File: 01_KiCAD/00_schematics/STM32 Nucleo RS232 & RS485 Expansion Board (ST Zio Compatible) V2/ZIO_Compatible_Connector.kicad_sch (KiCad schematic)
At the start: 15 parts, among them CN10 Conn_02x17_Odd_Even, CN7 Conn_02x10_Odd_Even, CN8 Conn_02x08_Odd_Even, CN9 Conn_02x15_Odd_Even, Q2 BSS84

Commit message: Finishing up the schematic aand created the board outline
Made some finishing touches to the schematic, updated all the symbol footprints and started to create the board.
Added missing 3D models for Phoenix 4-p RS485 connector and RS232 connector, also for Inolux LED.
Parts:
- CN10: footprint (none) -> SSW-117-23-F-D:SAMTEC_SSW-117-23-F-D
- CN7: footprint (none) -> SSW-110-23-X-D:SAMTEC_SSW-110-23-X-D
- CN8: footprint (none) -> SSW-108-23-F-D:SAMTEC_SSW-108-23-F-D
- renumbered R34 to R70, R35 to R71, R36 to R72, R37 to R73, R38 to R74, R39 to R75, R40 to R76, R41 to R77, R42 to R78, R43 to R79
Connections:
- net MCU_SHDN_N_1 renamed MCU_SHDN
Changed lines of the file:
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@@
 		)
 	)
-	(global_label "MCU_SHDN_N_1"
+	(global_label "MCU_SHDN"
 		(shape output)
 		(at 118.11 133.35 0)
@@
 		)
 		(property "Intersheetrefs" "${INTERSHEET_REFS}"
-			(at 135.7304 133.35 0)
+			(at 131.2552 133.35 0)
 			(effects
 				(font
@@
 		(on_board yes)
 		(dnp no)
-		(property "Reference" "R37"
+		(property "Reference" "R73"
 			(at 82.55 96.52 90)
 			(effects
@@
 			(project "STM32 Nucleo RS232 & RS485 Expansion Board (ST Zio Compatible) V2"
 				(path "/080f83b7-8913-48e8-ab8e-79cb12295542/067a36dd-1222-49fa-b4c7-0b289d0be8ff"
-					(reference "R37")
+					(reference "R73")
 					(unit 1)
 				)
@@
 		(on_board yes)
 		(dnp no)
-		(property "Reference" "R38"
+		(property "Reference" "R74"
 			(at 66.04 101.6 90)
 			(effects
@@
 			(project "STM32 Nucleo RS232 & RS485 Expansion Board (ST Zio Compatible) V2"
 				(path "/080f83b7-8913-48e8-ab8e-79cb12295542/067a36dd-1222-49fa-b4c7-0b289d0be8ff"
-					(reference "R38")
+					(reference "R74")
 					(unit 1)
 				)
@@
 		(on_board yes)
 		(dnp no)
-		(property "Reference" "R43"
+		(property "Reference" "R79"
 			(at 147.574 255.27 90)
 			(effects
@@
 			(project "STM32 Nucleo RS232 & RS485 Expansion Board (ST Zio Compatible) V2"
 				(path "/080f83b7-8913-48e8-ab8e-79cb12295542/067a36dd-1222-49fa-b4c7-0b289d0be8ff"
-					(reference "R43")
+					(reference "R79")
 					(unit 1)
 				)
@@
 			)
 		)
-		(property "Datasheet" "https://www.lcsc.com/datasheet/C7089189.pdf"
+		(property "Datasheet" "~"
 			(at 104.14 115.57 0)
 			(effects
@@
 			)
 		)
-		(property "Description" "Female Header 30 Position 2.54mm Pitch Dual Row Through Hole -55℃~+125℃"
+		(property "Description" "Generic connector, double row, 02x15, odd/even pin numbering scheme (row 1 odd numbers, row 2 even numbers), script generated (kicad-library-utils/schlib/autogen/connector/)"
 			(at 104.14 115.57 0)
 			(effects
@@
 		(on_board yes)
 		(dnp no)
-		(property "Reference" "R35"
+		(property "Reference" "R71"
 			(at 193.04 76.2 90)
 			(effects
@@
 			(project "STM32 Nucleo RS232 & RS485 Expansion Board (ST Zio Compatible) V2"
 				(path "/080f83b7-8913-48e8-ab8e-79cb12295542/067a36dd-1222-49fa-b4c7-0b289d0be8ff"
-					(reference "R35")
+					(reference "R71")
 					(unit 1)
 				)
@@
 		(on_board yes)
 		(dnp no)
-		(property "Reference" "R39"
+		(property "Reference" "R75"
 			(at 82.55 104.14 90)
 			(effects
@@
 			(project "STM32 Nucleo RS232 & RS485 Expansion Board (ST Zio Compatible) V2"
 				(path "/080f83b7-8913-48e8-ab8e-79cb12295542/067a36dd-1222-49fa-b4c7-0b289d0be8ff"
-					(reference "R39")
+					(reference "R75")
 					(unit 1)
 				)
@@
 		(on_board yes)
 		(dnp no)
-		(property "Reference" "R40"
+		(property "Reference" "R76"
 			(at 76.2 109.22 90)
 			(effects
@@
 			(project "STM32 Nucleo RS232 & RS485 Expansion Board (ST Zio Compatible) V2"
 				(path "/080f83b7-8913-48e8-ab8e-79cb12295542/067a36dd-1222-49fa-b4c7-0b289d0be8ff"
-					(reference "R40")
+					(reference "R76")
 					(unit 1)
 				)
@@
 		(on_board yes)
 		(dnp no)
-		(property "Reference" "R34"
+		(property "Reference" "R70"
 			(at 193.04 63.5 90)
 			(effects
@@
 			(project "STM32 Nucleo RS232 & RS485 Expansion Board (ST Zio Compatible) V2"
 				(path "/080f83b7-8913-48e8-ab8e-79cb12295542/067a36dd-1222-49fa-b4c7-0b289d0be8ff"
-					(reference "R34")
+					(reference "R70")
 					(unit 1)
 				)
@@
 		(dnp no)
 		(fields_autoplaced yes)
-		(property "Reference" "R41"
+		(property "Reference" "R77"
 			(at 139.7 228.5999 0)
 			(effects
@@
 			(project "STM32 Nucleo RS232 & RS485 Expansion Board (ST Zio Compatible) V2"
 				(path "/080f83b7-8913-48e8-ab8e-79cb12295542/067a36dd-1222-49fa-b4c7-0b289d0be8ff"
-					(reference "R41")
+					(reference "R77")
 					(unit 1)
 				)
@@
 			)
 		)
-		(property "Footprint" ""
+		(property "Footprint" "SSW-110-23-X-D:SAMTEC_SSW-110-23-X-D"
 			(at 181.61 64.77 0)
 			(effects
@@
 			)
 		)
-		(property "Datasheet" "https://www.lcsc.com/datasheet/C6236460.pdf"
+		(property "Datasheet" "~"
 			(at 181.61 64.77 0)
 			(effects
@@
 			)
 		)
-		(property "Description" "-55℃~+125℃ Through Hole 4.7A 20P 8.51mm 2.54mm 2 2.54mm Through Hole,P=2.54mm Headers, Receptacles, Female Sockets RoHS"
+		(property "Description" "Generic connector, double row, 02x10, odd/even pin numbering scheme (row 1 odd numbers, row 2 even numbers), script generated (kicad-library-utils/schlib/autogen/connector/)"
 			(at 181.61 64.77 0)
 			(effects
@@
 			)
 		)
-		(property "Footprint" ""
+		(property "Footprint" "SSW-108-23-F-D:SAMTEC_SSW-108-23-F-D"
 			(at 104.14 72.39 0)
 			(effects
@@
 			)
 		)
-		(property "Datasheet" "https://www.lcsc.com/datasheet/C7019040.pdf"
+		(property "Datasheet" "~"
 			(at 104.14 72.39 0)
 			(effects
@@
 			)
 		)
-		(property "Description" "-55℃~+125℃ Through Hole 4.7A 16P 8.51mm 2.54mm 2 2.54mm Through Hole,P=2.54mm Headers, Receptacles, Female Sockets RoHS"
+		(property "Description" "Generic connector, double row, 02x08, odd/even pin numbering scheme (row 1 odd numbers, row 2 even numbers), script generated (kicad-library-utils/schlib/autogen/connector/)"
 			(at 104.14 72.39 0)
 			(effects
@@
 		(dnp no)
 		(fields_autoplaced yes)
-		(property "Reference" "#PWR047"
+		(property "Reference" "#PWR067"
 			(at 92.71 88.9 0)
 			(effects
@@
 			(project ""
 				(path "/080f83b7-8913-48e8-ab8e-79cb12295542/067a36dd-1222-49fa-b4c7-0b289d0be8ff"
-					(reference "#PWR047")
+					(reference "#PWR067")
 					(unit 1)
 				)
@@
 		(on_board yes)
 		(dnp no)
-		(property "Reference" "R36"
+		(property "Reference" "R72"
 			(at 193.04 91.44 90)
 			(effects
@@
 			(project "STM32 Nucleo RS232 & RS485 Expansion Board (ST Zio Compatible) V2"
 				(path "/080f83b7-8913-48e8-ab8e-79cb12295542/067a36dd-1222-49fa-b4c7-0b289d0be8ff"
-					(reference "R36")
+					(reference "R72")
 					(unit 1)
 				)
@@
 			)
 		)
-		(property "Footprint" ""
+		(property "Footprint" "SSW-117-23-F-D:SAMTEC_SSW-117-23-F-D"
 			(at 181.61 113.03 0)
 			(effects
@@
 			)
 		)
-		(property "Datasheet" "https://www.lcsc.com/datasheet/C6501751.pdf"
+		(property "Datasheet" "~"
 			(at 181.61 113.03 0)
 			(effects
@@
 			)
 		)
-		(property "Description" "Female Header 34 Position 2.54mm Pitch Dual Row Through Hole -55℃~+125℃"
+		(property "Description" "Generic connector, double row, 02x17, odd/even pin numbering scheme (row 1 odd numbers, row 2 even numbers), script generated (kicad-library-utils/schlib/autogen/connector/)"
 			(at 181.61 113.03 0)
 			(effects
@@
 		(dnp no)
 		(fields_autoplaced yes)
-		(property "Reference" "R42"
+		(property "Reference" "R78"
 			(at 162.56 228.5999 0)
 			(effects
@@
 			(project "STM32 Nucleo RS232 & RS485 Expansion Board (ST Zio Compatible) V2"
 				(path "/080f83b7-8913-48e8-ab8e-79cb12295542/067a36dd-1222-49fa-b4c7-0b289d0be8ff"
-					(reference "R42")
+					(reference "R78")
 					(unit 1)
 				)

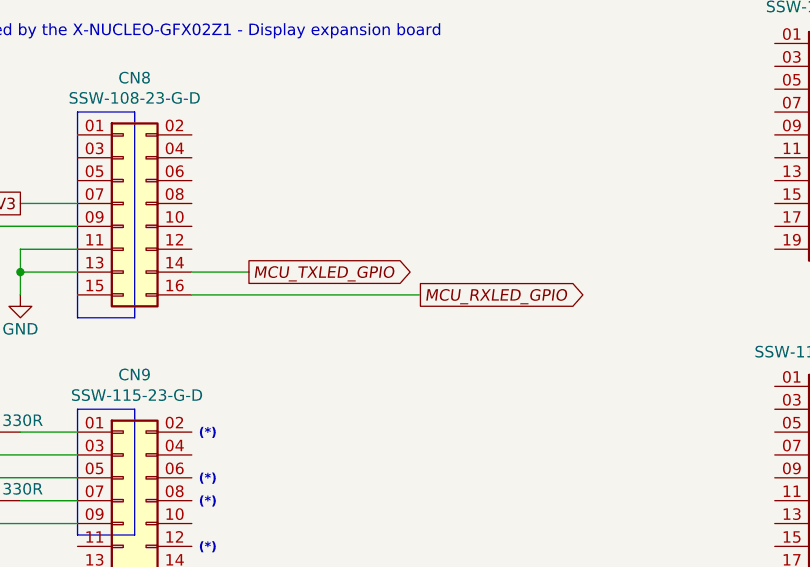
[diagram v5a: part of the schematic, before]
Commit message: Updated footprints and added components to PCB
Added some additional components to the board. Changed the footprint of the 3-pin Jumper so the bottom silkscreen text doesnlt overlap with the Dual Schmidt Trigger IC's SN74LVC2G14
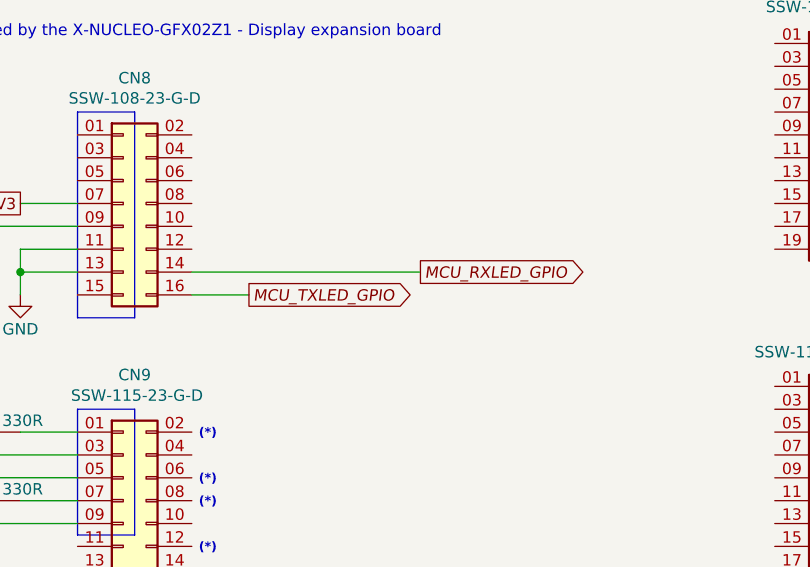
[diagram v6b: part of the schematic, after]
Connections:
- net MCU_RXLED_GPIO: now also CN8.14 (Pin_14); no longer CN8.16 (Pin_16)
- net MCU_TXLED_GPIO: now also CN8.16 (Pin_16); no longer CN8.14 (Pin_14)
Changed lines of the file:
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@@
 	(wire
 		(pts
-			(xy 217.17 64.77) (xy 203.2 64.77)
+			(xy 111.76 82.55) (xy 118.11 82.55)
 		)
 		(stroke
@@
 	(wire
 		(pts
-			(xy 111.76 80.01) (xy 118.11 80.01)
+			(xy 217.17 64.77) (xy 203.2 64.77)
 		)
 		(stroke
@@
 	(wire
 		(pts
+			(xy 111.76 80.01) (xy 137.16 80.01)
+		)
+		(stroke
+			(width 0)
+			(type default)
+		)
+	)
+	(wire
+		(pts
 			(xy 208.28 92.71) (xy 203.2 92.71)
 		)
@@
 		)
 	)
-	(wire
-		(pts
-			(xy 111.76 82.55) (xy 137.16 82.55)
-		)
-		(stroke
-			(width 0)
-			(type default)
-		)
-	)
 	(global_label "L3-TXD"
 		(shape output)
@@
 	(global_label "MCU_RXLED_GPIO"
 		(shape output)
-		(at 137.16 82.55 0)
+		(at 137.16 80.01 0)
 		(fields_autoplaced yes)
 		(effects
@@
 		)
 		(property "Intersheetrefs" "${INTERSHEET_REFS}"
-			(at 156.5342 82.55 0)
+			(at 156.5342 80.01 0)
 			(effects
 				(font
@@
 	(global_label "MCU_TXLED_GPIO"
 		(shape output)
-		(at 118.11 80.01 0)
+		(at 118.11 82.55 0)
 		(fields_autoplaced yes)
 		(effects
@@
 		)
 		(property "Intersheetrefs" "${INTERSHEET_REFS}"
-			(at 137.1818 80.01 0)
+			(at 137.1818 82.55 0)
 			(effects
 				(font
@@
 			)
 		)
-		(property "Datasheet" "https://www.lcsc.com/datasheet/C105881.pdf"
+		(property "Datasheet" "~"
 			(at 87.63 97.79 0)
 			(effects
@@
 			)
 		)
-		(property "Description" "100mW 330Ω 75V Thick Film Resistor ±100ppm/℃ ±1% 0603 Chip Resistor - Surface Mount RoHS"
+		(property "Description" "Resistor"
 			(at 87.63 97.79 0)
 			(effects
@@
 			)
 		)
-		(property "Datasheet" "https://www.lcsc.com/datasheet/C105881.pdf"
+		(property "Datasheet" "~"
 			(at 71.12 102.87 0)
 			(effects
@@
 			)
 		)
-		(property "Description" "100mW 330Ω 75V Thick Film Resistor ±100ppm/℃ ±1% 0603 Chip Resistor - Surface Mount RoHS"
+		(property "Description" "Resistor"
 			(at 71.12 102.87 0)
 			(effects
@@
 			)
 		)
-		(property "Datasheet" "https://www.lcsc.com/datasheet/C22548.pdf"
+		(property "Datasheet" "~"
 			(at 154.94 252.73 0)
 			(effects
@@
 			)
 		)
-		(property "Description" "100mW 1kΩ 75V Thick Film Resistor ±100ppm/℃ ±1% 0603 Chip Resistor - Surface Mount RoHS"
+		(property "Description" "Resistor"
 			(at 154.94 252.73 0)
 			(effects
@@
 			)
 		)
-		(property "Datasheet" "https://www.lcsc.com/datasheet/C82079.pdf"
+		(property "Datasheet" "http://assets.nexperia.com/documents/data-sheet/BSS84.pdf"
 			(at 110.49 228.6 0)
 			(effects
@@
 			)
 		)
-		(property "Description" "P-Channel 50V 130mA 225mW Surface Mount SOT-23"
+		(property "Description" "-0.13A Id, -50V Vds, P-Channel MOSFET, SOT-23"
 			(at 105.41 232.41 0)
 			(effects
@@
 			)
 		)
-		(property "Datasheet" "https://www.lcsc.com/datasheet/C105881.pdf"
+		(property "Datasheet" "~"
 			(at 198.12 77.47 0)
 			(effects
@@
 			)
 		)
-		(property "Description" "100mW 330Ω 75V Thick Film Resistor ±100ppm/℃ ±1% 0603 Chip Resistor - Surface Mount RoHS"
+		(property "Description" "Resistor"
 			(at 198.12 77.47 0)
 			(effects
@@
 			)
 		)
-		(property "Datasheet" "https://www.lcsc.com/datasheet/C105881.pdf"
+		(property "Datasheet" "~"
 			(at 87.63 105.41 0)
 			(effects
@@
 			)
 		)
-		(property "Description" "100mW 330Ω 75V Thick Film Resistor ±100ppm/℃ ±1% 0603 Chip Resistor - Surface Mount RoHS"
+		(property "Description" "Resistor"
 			(at 87.63 105.41 0)
 			(effects
@@
 			)
 		)
-		(property "Datasheet" "https://www.lcsc.com/datasheet/C105881.pdf"
+		(property "Datasheet" "~"
 			(at 71.12 107.95 0)
 			(effects
@@
 			)
 		)
-		(property "Description" "100mW 330Ω 75V Thick Film Resistor ±100ppm/℃ ±1% 0603 Chip Resistor - Surface Mount RoHS"
+		(property "Description" "Resistor"
 			(at 71.12 107.95 0)
 			(effects
@@
 			)
 		)
-		(property "Datasheet" "https://www.lcsc.com/datasheet/C105881.pdf"
+		(property "Datasheet" "~"
 			(at 198.12 64.77 0)
 			(effects
@@
 			)
 		)
-		(property "Description" "100mW 330Ω 75V Thick Film Resistor ±100ppm/℃ ±1% 0603 Chip Resistor - Surface Mount RoHS"
+		(property "Description" "Resistor"
 			(at 198.12 64.77 0)
 			(effects
@@
 			)
 		)
-		(property "Datasheet" "https://www.lcsc.com/datasheet/C98220.pdf"
+		(property "Datasheet" "~"
 			(at 137.16 231.14 0)
 			(effects
@@
 			)
 		)
-		(property "Description" "100mW 10kΩ 75V Thick Film Resistor ±100ppm/℃ ±1% 0603 Chip Resistor - Surface Mount RoHS"
+		(property "Description" "Resistor"
 			(at 137.16 231.14 0)
 			(effects
@@
 			)
 		)
-		(property "Datasheet" "https://www.lcsc.com/datasheet/C105881.pdf"
+		(property "Datasheet" "~"
 			(at 198.12 92.71 0)
 			(effects
@@
 			)
 		)
-		(property "Description" "100mW 330Ω 75V Thick Film Resistor ±100ppm/℃ ±1% 0603 Chip Resistor - Surface Mount RoHS"
+		(property "Description" "Resistor"
 			(at 198.12 92.71 0)
 			(effects
@@
 			)
 		)
-		(property "Datasheet" "https://www.lcsc.com/datasheet/C108078.pdf"
+		(property "Datasheet" "~"
 			(at 160.02 231.14 0)
 			(effects
@@
 			)
 		)
-		(property "Description" "100mW 3.3kΩ 75V Thick Film Resistor ±100ppm/℃ ±1% 0603 Chip Resistor - Surface Mount RoHS"
+		(property "Description" "Resistor"
 			(at 160.02 231.14 0)
 			(effects

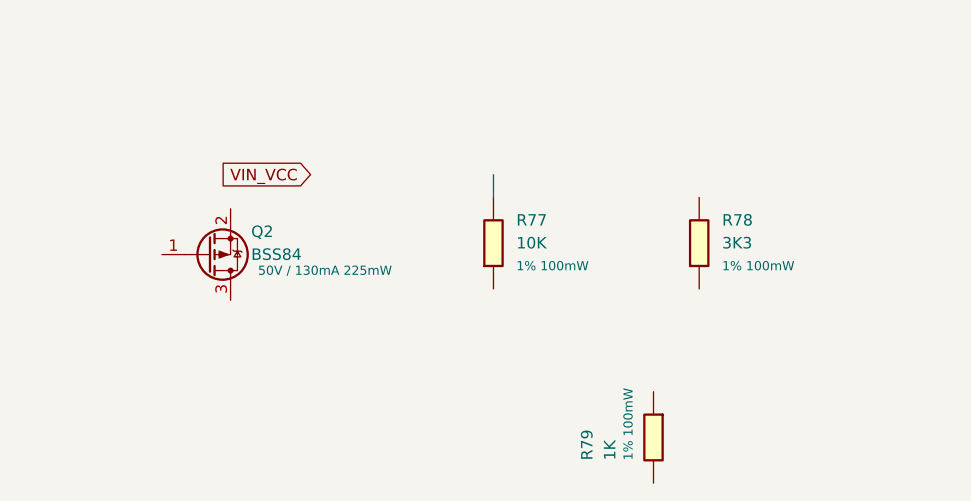
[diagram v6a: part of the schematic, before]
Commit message: Changed schmitt trigger
changed the schmitt trigger for hex-schmitt trigger variant to simpify design and reduce components
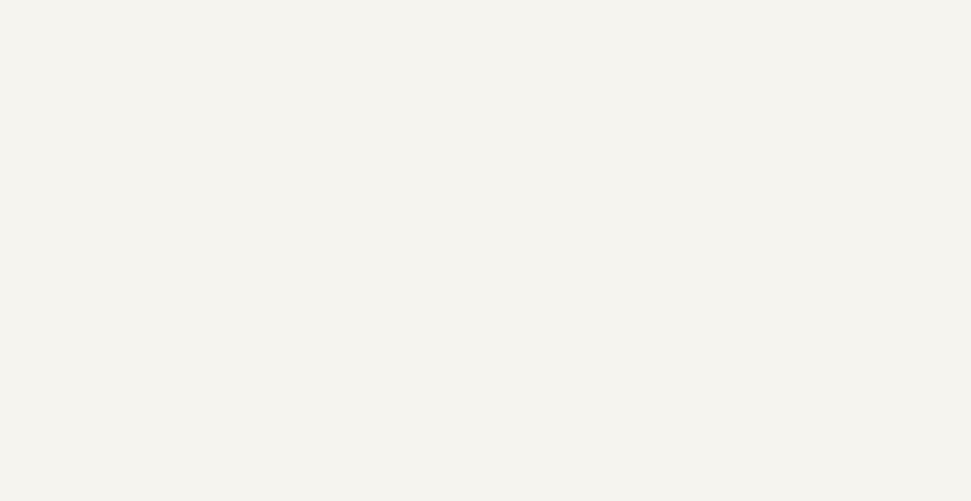
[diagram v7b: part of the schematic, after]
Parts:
- removed Q2: BSS84, Package_TO_SOT_SMD:SOT-23, symbol Transistor_FET:BSS84
- removed R77: 10K, PCM_fab:R_0603, symbol PCM_fab:R_0603
- removed R78: 3K3, PCM_fab:R_0603, symbol PCM_fab:R_0603
- removed R79: 1K, PCM_fab:R_0603, symbol PCM_fab:R_0603
